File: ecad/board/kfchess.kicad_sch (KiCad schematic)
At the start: 7 parts, among them U1 KF128-5_08-2P, U2 DB129VG-5_08-4P-GN-S, U3 DB129VG-5_08-4P-GN-S, U4 Teensy4.1, U9 24_243_2

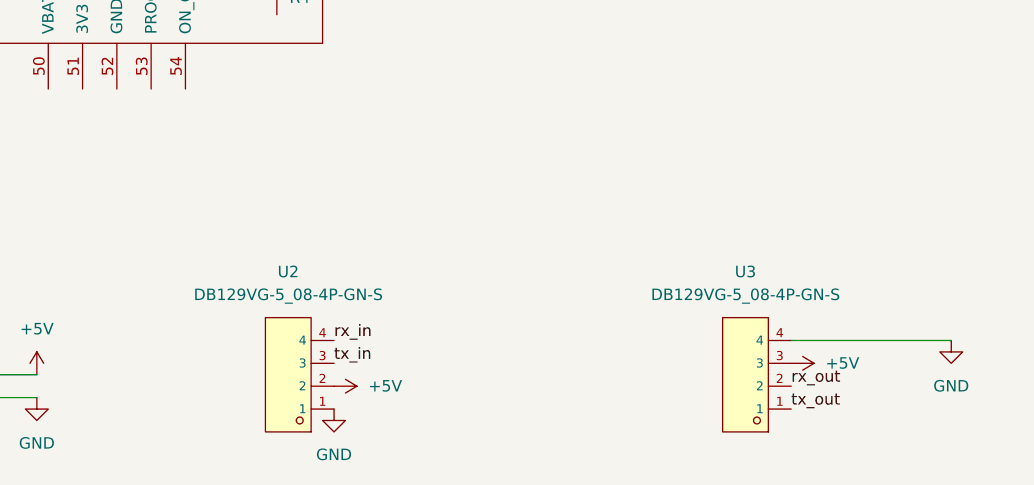
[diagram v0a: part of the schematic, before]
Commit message: Fixed upside down cross board screw terminals
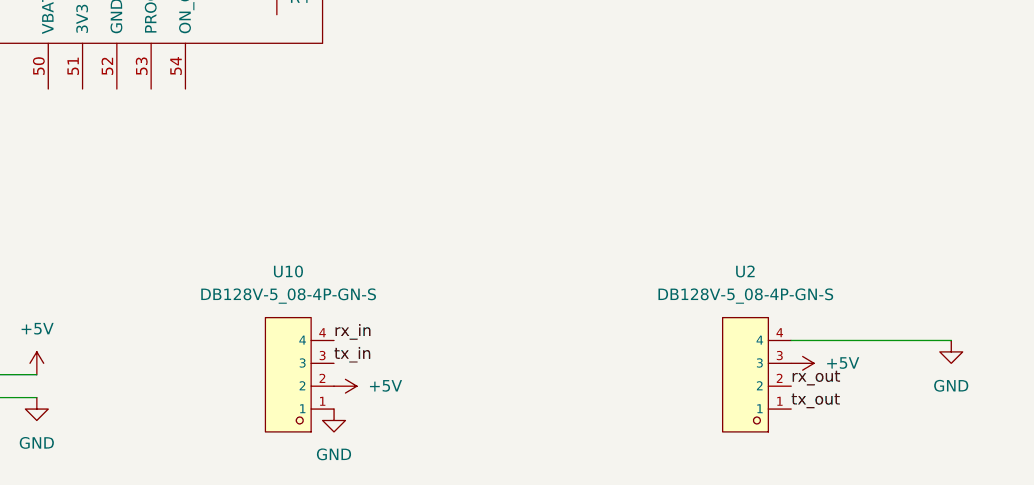
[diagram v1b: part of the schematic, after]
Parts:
- removed U2, U3: DB129VG-5_08-4P-GN-S, footprint:CONN-TH_4P-P5.08_DB129VG-5.08-4P-GN-S, symbol DB129VG-5_08-4P-GN-S:DB129VG-5_08-4P-GN-S
- added U10, U2: DB128V-5_08-4P-GN-S, footprint:CONN-TH_4P-P5.08_DIBO_DB128V-5.08, symbol DB128V-5_08-4P-GN-S:DB128V-5_08-4P-GN-S
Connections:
- net +5V: now also U10.2, U2.3
- net GND: now also U10.1, U2.4
- net rx_in: now also U10.4
- net rx_out: now also U2.2
- net tx_in: now also U10.3
- net tx_out: now also U2.1
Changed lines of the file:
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@@
-	)
-	(symbol
-		(lib_id "DB129VG-5_08-4P-GN-S:DB129VG-5_08-4P-GN-S")
-		(at 142.24 154.94 180)
-		(unit 1)
-		(exclude_from_sim no)
-		(in_bom yes)
-		(on_board yes)
-		(dnp no)
-		(fields_autoplaced yes)
-		(property "Reference" "U3"
-			(at 142.24 143.51 0)
-			(effects
-				(font
-					(size 1.27 1.27)
-				)
-			)
-		)
-		(property "Value" "DB129VG-5_08-4P-GN-S"
-			(at 142.24 146.05 0)
-			(effects
-				(font
-					(size 1.27 1.27)
-				)
-			)
-		)
-		(property "Footprint" "footprint:CONN-TH_4P-P5.08_DB129VG-5.08-4P-GN-S"
-			(at 142.24 144.78 0)
-			(effects
-				(font
-					(size 1.27 1.27)
-					(italic yes)
-				)
-				(hide yes)
-			)
-		)
-		(property "Datasheet" "https://atta.szlcsc.com/upload/public/pdf/source/20221104/14E80596629FA66A7247B0FAA60359B7.pdf"
-			(at 144.526 155.067 0)
-			(effects
-				(font
-					(size 1.27 1.27)
-				)
-				(justify left)
-				(hide yes)
-			)
-		)
-		(property "Description" ""
-			(at 142.24 154.94 0)
-			(effects
-				(font
-					(size 1.27 1.27)
-				)
-				(hide yes)
-			)
-		)
-		(property "LCSC" "C2981774"
-			(at 142.24 154.94 0)
-			(effects
-				(font
-					(size 1.27 1.27)
-				)
-				(hide yes)
-			)
-		)
-		(pin "1"
-		)
-		(pin "2"
-		)
-		(pin "3"
-		)
-		(pin "4"
-		)
-		(instances
-			(project "kfchess"
-				(path "/d706098d-c574-48d0-bc99-bc3e7fab44dd"
-					(reference "U3")
-					(unit 1)
-				)
-			)
-		)
 	)
 	(symbol
@@
 	)
 	(symbol
-		(lib_id "DB129VG-5_08-4P-GN-S:DB129VG-5_08-4P-GN-S")
+		(lib_id "DB128V-5_08-4P-GN-S:DB128V-5_08-4P-GN-S")
 		(at 91.44 154.94 180)
 		(unit 1)
@@
 		(dnp no)
 		(fields_autoplaced yes)
-		(property "Reference" "U2"
+		(property "Reference" "U10"
 			(at 91.44 143.51 0)
 			(effects
@@
 			)
 		)
-		(property "Value" "DB129VG-5_08-4P-GN-S"
+		(property "Value" "DB128V-5_08-4P-GN-S"
 			(at 91.44 146.05 0)
 			(effects
@@
 			)
 		)
-		(property "Footprint" "footprint:CONN-TH_4P-P5.08_DB129VG-5.08-4P-GN-S"
+		(property "Footprint" "footprint:CONN-TH_4P-P5.08_DIBO_DB128V-5.08"
 			(at 91.44 144.78 0)
 			(effects
@@
 			)
 		)
-		(property "Datasheet" "https://atta.szlcsc.com/upload/public/pdf/source/20221104/14E80596629FA66A7247B0FAA60359B7.pdf"
+		(property "Datasheet" "https://atta.szlcsc.com/upload/public/pdf/source/20211116/A787F5746A5FC39810745D8FDCF241F0.pdf"
 			(at 93.726 155.067 0)
 			(effects
@@
 			)
 		)
-		(property "LCSC" "C2981774"
+		(property "LCSC" "C2915641"
 			(at 91.44 154.94 0)
 			(effects
@@
 			)
 		)
+		(pin "2"
+		)
+		(pin "3"
+		)
 		(pin "1"
-		)
-		(pin "2"
-		)
-		(pin "3"
 		)
 		(pin "4"
@@
 			(project ""
 				(path "/d706098d-c574-48d0-bc99-bc3e7fab44dd"
-					(reference "U2")
+					(reference "U10")
 					(unit 1)
 				)
@@
 					(unit 1)
 				)
+			)
+		)
+	)
+	(symbol
+		(lib_id "DB128V-5_08-4P-GN-S:DB128V-5_08-4P-GN-S")
+		(at 142.24 154.94 180)
+		(unit 1)
+		(exclude_from_sim no)
+		(in_bom yes)
+		(on_board yes)
+		(dnp no)
+		(fields_autoplaced yes)
+		(property "Reference" "U2"
+			(at 142.24 143.51 0)
+			(effects
+				(font
+					(size 1.27 1.27)
+				)
+			)
+		)
+		(property "Value" "DB128V-5_08-4P-GN-S"
+			(at 142.24 146.05 0)
+			(effects
+				(font
+					(size 1.27 1.27)
+				)
+			)
+		)
+		(property "Footprint" "footprint:CONN-TH_4P-P5.08_DIBO_DB128V-5.08"
+			(at 142.24 144.78 0)
+			(effects
+				(font
+					(size 1.27 1.27)
+					(italic yes)
+				)
+				(hide yes)
+			)
+		)
+		(property "Datasheet" "https://atta.szlcsc.com/upload/public/pdf/source/20211116/A787F5746A5FC39810745D8FDCF241F0.pdf"
+			(at 144.526 155.067 0)
+			(effects
+				(font
+					(size 1.27 1.27)
+				)
+				(justify left)
+				(hide yes)
+			)
+		)
+		(property "Description" ""
+			(at 142.24 154.94 0)
+			(effects
+				(font
+					(size 1.27 1.27)
+				)
+				(hide yes)
+			)
+		)
+		(property "LCSC" "C2915641"
+			(at 142.24 154.94 0)
+			(effects
+				(font
+					(size 1.27 1.27)
+				)
+				(hide yes)
+			)
+		)
+		(pin "2"
+		)
+		(pin "3"
+		)
+		(pin "1"
+		)
+		(pin "4"
+		)
+		(instances
+			(project "kfchess"
+				(path "/d706098d-c574-48d0-bc99-bc3e7fab44dd"
+					(reference "U2")
+					(unit 1)
+				)
